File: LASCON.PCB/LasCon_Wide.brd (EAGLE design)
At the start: 44.4 x 28 mm, 11 parts

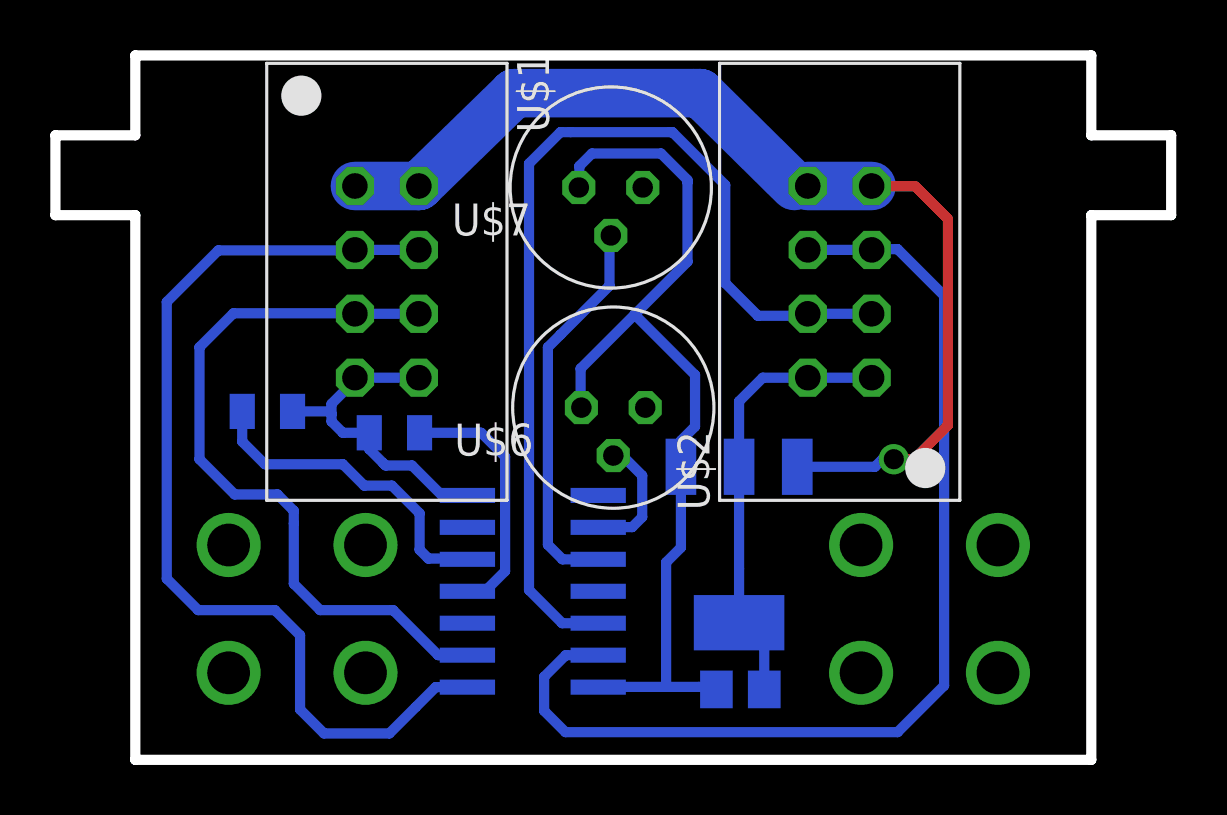
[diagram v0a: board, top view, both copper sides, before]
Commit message: LasCon, KW2 Frontend
Exported LasCon for Jeff, made "wide" version for milling test.
Schematic for KW2 front end in progress, missing F and ant connector.
Updated KW2 and GW libs with frontend parts
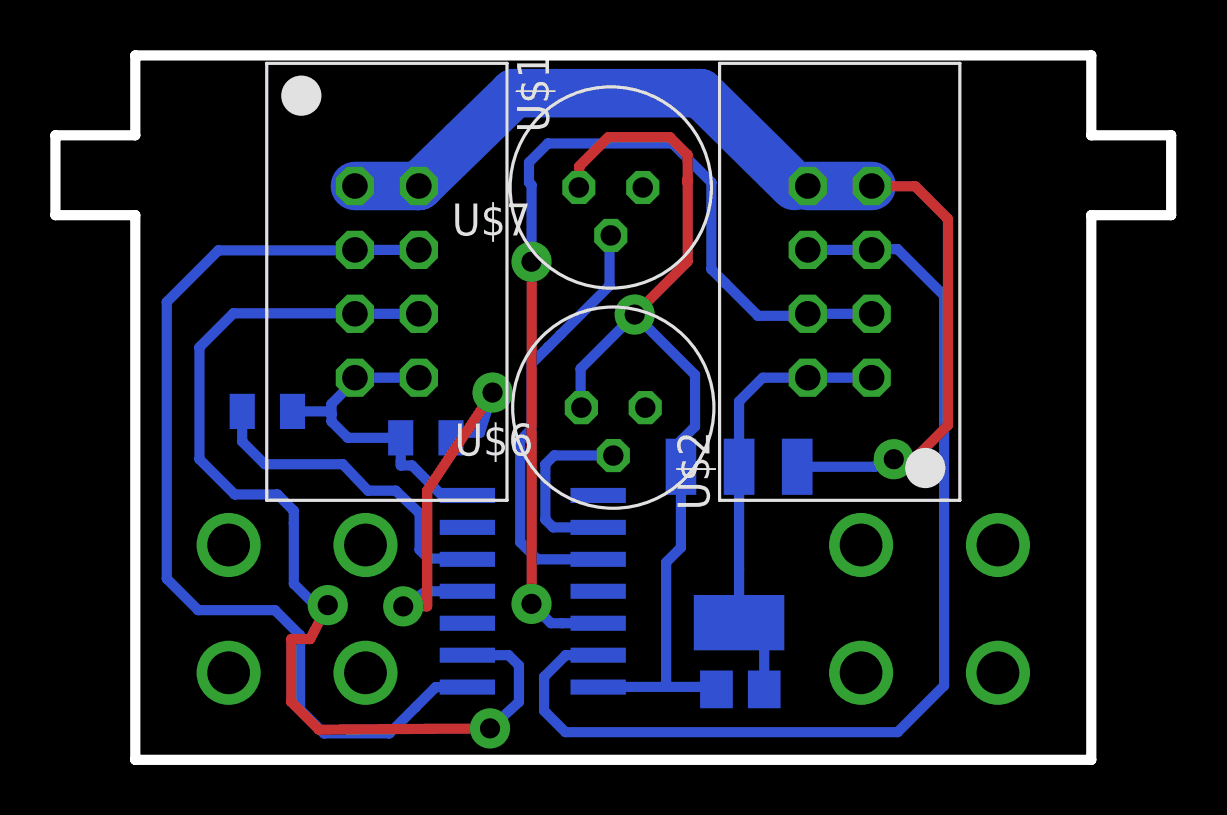
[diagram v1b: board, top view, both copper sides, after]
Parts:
- moved U$4 1.27 mm to (-7.45, -6.20)
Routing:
- net N$6: track 29.3 -> 41.4 mm, vias 0 -> 2
- net N$9: track 10.2 -> 18.4 mm, vias 0 -> 2
- net N$2: track 5.05 -> 7.28 mm
- net N$3: track 16.0 -> 17.5 mm
- net +3V3: track 37.6 -> 38.8 mm, vias 0 -> 1
- net N$8: track 39.7 -> 39.4 mm, vias 0 -> 2
